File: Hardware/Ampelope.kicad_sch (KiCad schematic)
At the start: 127 parts, among them J1 Eurorack_10_pin_power, J10 Audio1_Out, J11 Audio2_Out, J12 Audio3_Out, J13 Audio4_Out, J14 Env1_Out, J15 Env2_Out, J16 Env3_Out, J17 Env4_Out, J18 SWD_Header, J19 USB_B_Micro, J2 Gate1_In, J3 Gate2_In, J4 Gate3_In, J5 Gate4_In, J6 Audio1_In, J7 Audio2_In, J8 Audio3_In, J9 Audio4_In, Q1 MMBT3904, Q2 MMBT3904, Q3 MMBT3904, Q4 MMBT3904, SW1 SW_SPDT_MSM, SW2 SW_SPDT_MSM, SW3 SW_SPDT_MSM, SW4 SW_SPDT_MSM, U1 STM32G431RB, U2 AS3364, U3 LM1117-3.3, U4 TL074, U5 TL074, U6 TL074, Y1 8MHz 20pF

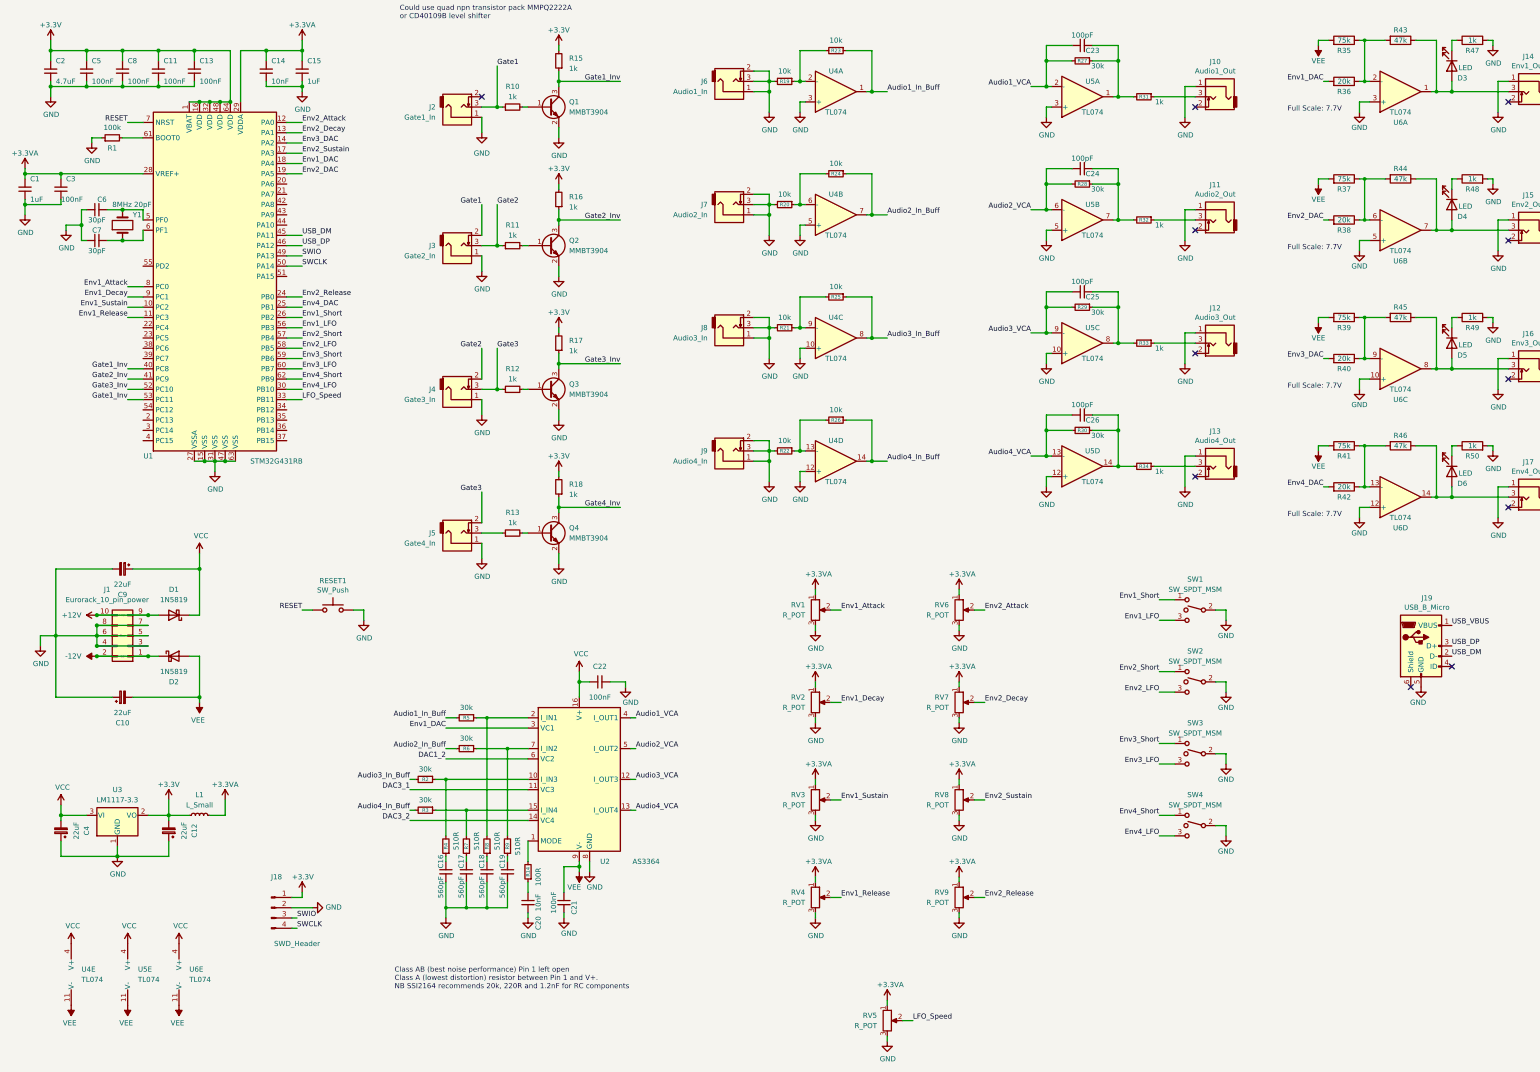
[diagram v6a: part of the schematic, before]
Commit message: Preliminary pcb layout preparation
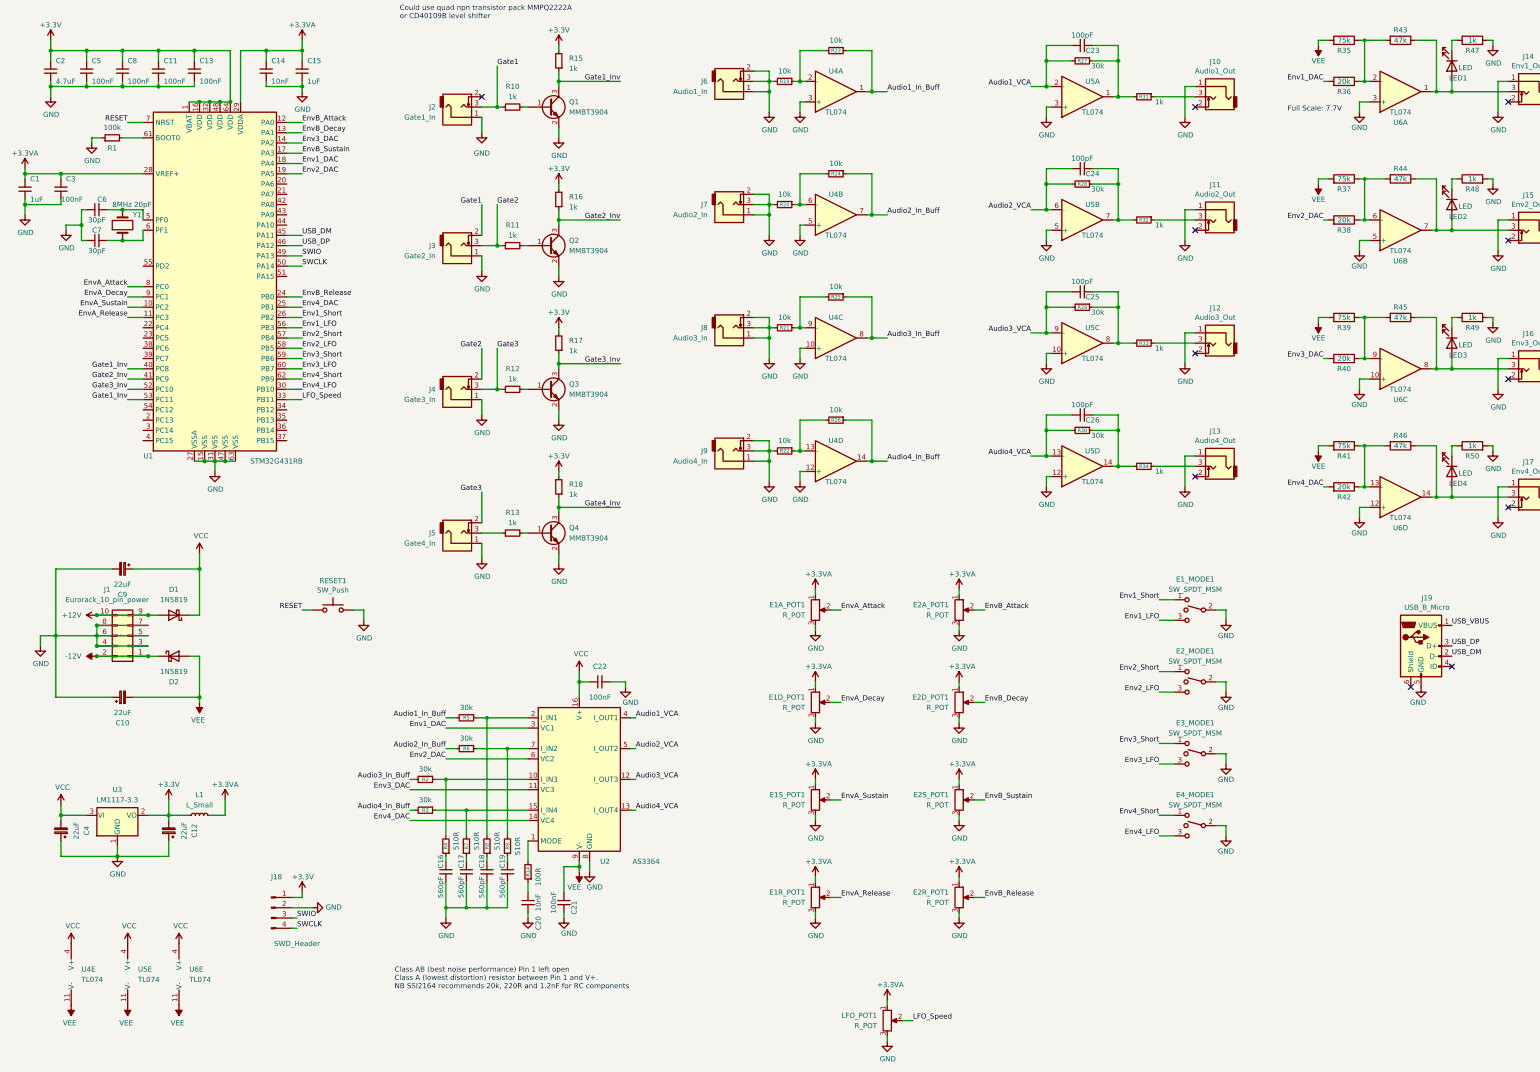
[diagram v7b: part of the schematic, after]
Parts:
- C1, C11, C13, C14, C15, C16, C17, C18, C19, C2, C20, C21, C22, C23, C24, C25, C26, C3, C5, C6, C7, C8: footprint Capacitors_SMD:C_0603_HandSoldering -> Capacitor_SMD:C_0603_1608Metric_Pad1.08x0.95mm_HandSolder
- L1: footprint Inductors_SMD:L_0805_HandSoldering -> Inductor_SMD:L_0805_2012Metric_Pad1.05x1.20mm_HandSolder
- LED1: renamed from D3; footprint LEDs:LED_D3.0mm -> LED_THT:LED_D3.0mm
- LED2: renamed from D4; footprint LEDs:LED_D3.0mm -> LED_THT:LED_D3.0mm
- LED3: renamed from D5; footprint LEDs:LED_D3.0mm -> LED_THT:LED_D3.0mm
- LED4: renamed from D6; footprint LEDs:LED_D3.0mm -> LED_THT:LED_D3.0mm
- R1, R10, R11, R12, R13, R14, R15, R16, R17, R18, R19, R2, R20, R21, R22, R23, R24, R25, R26, R27, R28, R29, R3, R30, R31, R32, R33, R34, R35, R36, R37, R38, R39, R4, R40, R41, R42, R43, R44, R45, R46, R47, R48, R49, R5, R50, R6, R7, R8, R9: footprint Resistors_SMD:R_0603_HandSoldering -> Resistor_SMD:R_0603_1608Metric_Pad0.98x0.95mm_HandSolder
- U3: footprint TO_SOT_Packages_SMD:SOT-223-3_TabPin2 -> Package_TO_SOT_SMD:SOT-223-3_TabPin2
- Y1: footprint Crystals:Crystal_SMD_5032-2pin_5.0x3.2mm_HandSoldering -> Crystal:Crystal_SMD_5032-2Pin_5.0x3.2mm_HandSoldering
- renumbered RV1 to E1A_POT1, RV2 to E1D_POT1, RV4 to E1R_POT1, RV3 to E1S_POT1, SW1 to E1_MODE1, RV6 to E2A_POT1, RV7 to E2D_POT1, RV9 to E2R_POT1, RV8 to E2S_POT1, SW2 to E2_MODE1, SW3 to E3_MODE1, SW4 to E4_MODE1, RV5 to LFO_POT1
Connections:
- net DAC1_2 is gone; now on net Env2_DAC: U2.6 (VC2)
- net DAC3_1 is gone; now on net Env3_DAC: U2.11 (VC3)
- net DAC3_2 is gone; now on net Env4_DAC: U2.14 (VC4)
- net Env1_Attack renamed EnvA_Attack
- net Env1_Decay renamed EnvA_Decay
- net Env1_Release renamed EnvA_Release
- net Env1_Sustain renamed EnvA_Sustain
- net Env2_Attack renamed EnvB_Attack
- net Env2_Decay renamed EnvB_Decay
- net Env2_Release renamed EnvB_Release
- net Env2_Sustain renamed EnvB_Sustain

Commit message: Split PCBs into separate control and component boards
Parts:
- removed E1A_POT1, E1D_POT1, E1R_POT1, E1S_POT1, E2A_POT1, E2D_POT1, E2R_POT1, E2S_POT1, LFO_POT1: R_POT, Custom_Footprints:Alpha_9mm_Potentiometer_Aligned, symbol Encoder:R_POT
- removed E1_MODE1, E2_MODE1, E3_MODE1, E4_MODE1: SW_SPDT_MSM, Custom_Footprints:SPDT_SubMiniature_Aligned, symbol Switch:SW_SPDT_MSM
- removed J1: Eurorack_10_pin_power, Custom_Footprints:Eurorack_10_pin_header, symbol Eurorack Header:Eurorack_10_pin_power
- removed J10: Audio1_Out, Custom_Footprints:THONKICONN_hole, symbol thonkiconn:AudioJack2_Ground_Switch
- removed J11: Audio2_Out, Custom_Footprints:THONKICONN_hole, symbol thonkiconn:AudioJack2_Ground_Switch
- removed J12: Audio3_Out, Custom_Footprints:THONKICONN_hole, symbol thonkiconn:AudioJack2_Ground_Switch
- removed J13: Audio4_Out, Custom_Footprints:THONKICONN_hole, symbol thonkiconn:AudioJack2_Ground_Switch
- removed J14: Env1_Out, Custom_Footprints:THONKICONN_hole, symbol thonkiconn:AudioJack2_Ground_Switch
- removed J15: Env2_Out, Custom_Footprints:THONKICONN_hole, symbol thonkiconn:AudioJack2_Ground_Switch
- removed J16: Env3_Out, Custom_Footprints:THONKICONN_hole, symbol thonkiconn:AudioJack2_Ground_Switch
- removed J17: Env4_Out, Custom_Footprints:THONKICONN_hole, symbol thonkiconn:AudioJack2_Ground_Switch
- removed J2: Gate1_In, Custom_Footprints:THONKICONN_hole, symbol thonkiconn:AudioJack2_Ground_Switch
- removed J3: Gate2_In, Custom_Footprints:THONKICONN_hole, symbol thonkiconn:AudioJack2_Ground_Switch
- removed J4: Gate3_In, Custom_Footprints:THONKICONN_hole, symbol thonkiconn:AudioJack2_Ground_Switch
- removed J5: Gate4_In, Custom_Footprints:THONKICONN_hole, symbol thonkiconn:AudioJack2_Ground_Switch
- removed J6: Audio1_In, Custom_Footprints:THONKICONN_hole, symbol thonkiconn:AudioJack2_Ground_Switch
- removed J7: Audio2_In, Custom_Footprints:THONKICONN_hole, symbol thonkiconn:AudioJack2_Ground_Switch
- removed J8: Audio3_In, Custom_Footprints:THONKICONN_hole, symbol thonkiconn:AudioJack2_Ground_Switch
- removed J9: Audio4_In, Custom_Footprints:THONKICONN_hole, symbol thonkiconn:AudioJack2_Ground_Switch
- removed LED1, LED2, LED3, LED4: LED, LED_THT:LED_D3.0mm, symbol Device:LED
- removed R48, R49, R50: 1k, Resistor_SMD:R_0603_1608Metric_Pad0.98x0.95mm_HandSolder, symbol Device:R
- added J? (x2): Conn_01x12_Male, symbol Connector:Conn_01x12_Male
- added J? (x2): Conn_01x08_Male, Pin_Headers:Pin_Header_Straight_1x08_Pitch2.54mm, symbol Connector:Conn_01x08_Male
- added J?: Eurorack_16_pin_power, symbol Eurorack Header:Eurorack_16_pin_power
- added R? (x3): 1k, Resistor_SMD:R_0603_1608Metric_Pad0.98x0.95mm_HandSolder, symbol Device:R
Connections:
- net +12V: now also J?.1 (Pin_1); no longer D1.2 (A)
- net -12V: now also J?.9 (Pin_9); no longer D2.1 (K)
- net Env1_LFO: now also J?.10 (Pin_10)
- net Env1_Short: now also J?.9 (Pin_9)
- net Env2_LFO: now also J?.12 (Pin_12)
- net Env2_Short: now also J?.11 (Pin_11)
- net Env3_LFO: now also J?.7 (Pin_7)
- net Env3_Short: now also J?.6 (Pin_6)
- net Env4_LFO: now also J?.9 (Pin_9)
- net Env4_Short: now also J?.8 (Pin_8)
- net EnvA_Attack: now also J?.5 (Pin_5)
- net EnvA_Decay: now also J?.6 (Pin_6)
- net EnvA_Release: now also J?.8 (Pin_8)
- net EnvA_Sustain: now also J?.7 (Pin_7)
- net EnvB_Attack: now also J?.2 (Pin_2)
- net EnvB_Decay: now also J?.3 (Pin_3)
- net EnvB_Release: now also J?.5 (Pin_5)
- net EnvB_Sustain: now also J?.4 (Pin_4)
- net GND: now also J?.3 (Pin_3), J?.4 (Pin_4), J?.5 (Pin_5), J?.6 (Pin_6), J?.7 (Pin_7), J?.8 (Pin_8); no longer R19.2, R20.2, R21.2, R22.2, R47.2
- net LFO_Speed: now also J?.1 (Pin_1)
- net Audio3_Out: now reaches R33.1
- net Audio3_Out: now also J?.3 (Pin_3)
- net Audio4_Out: now reaches R34.1
- net Audio4_Out: now also J?.4 (Pin_4)
- net Env1_Out: now reaches R43.1, U6.1
- net Env1_Out: now also R47.1, J?.2 (Pin_2)
- net Env3_Out: now reaches R45.1, U6.8
- net Env3_Out: now also J?.6 (Pin_6), R?.1
- net Env4_Out: now reaches R46.1, U6.14
- net Env4_Out: now also J?.8 (Pin_8), R?.1
- net Gate4_In: now reaches R13.1
- net Gate4_In: now also J?.4 (Pin_4)
- net Env2_Out: now reaches R44.1, U6.7
- net Env2_Out: now also J?.4 (Pin_4), R?.1
- net Audio1_Out: now reaches R31.1
- net Audio1_Out: now also J?.1 (Pin_1)
- net Audio2_Out: now reaches R32.1
- net Audio2_Out: now also J?.2 (Pin_2)
- net Gate1 renamed Gate1_In
- net Gate1_In: now also J?.1 (Pin_1)
- net Gate2 renamed Gate2_In
- net Gate2_In: now also J?.2 (Pin_2)
- net Gate3 renamed Gate3_In
- net Gate3_In: now also J?.3 (Pin_3)
- new net: D2.1 (K), J?.10 (Pin_10)
- new net: D1.2 (A), J?.2 (Pin_2)
- new net Audio1_In: J?.5 (Pin_5), R19.2
- new net Audio2_In: J?.6 (Pin_6), R20.2
- new net Audio3_In: J?.7 (Pin_7), R21.2
- new net Audio4_In: J?.8 (Pin_8), R22.2
- new net Gate_In: J?.15 (Pin_15), J?.16 (Pin_16)
- new net Led1_Out: J?.1 (Pin_1), R47.2
- new net Led2_Out: J?.3 (Pin_3), R?.2
- new net Led3_Out: J?.5 (Pin_5), R?.2
- new net Led4_Out: J?.7 (Pin_7), R?.2
- no-connect marks 11 -> 2
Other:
- moved on the sheet: C10, R47
